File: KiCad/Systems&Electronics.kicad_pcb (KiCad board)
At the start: 2 copper layers, 182.4 x 143.2 mm, 53 parts, among them J1 Pressure Transducer, J12 Screw_Terminal_01x02, J13 Screw_Terminal_01x03, J2 Pressure Transducer, J3 Pressure Transducer, J4 Pressure Transducer, J5 Pressure Transducer, J6 Pressure Transducer

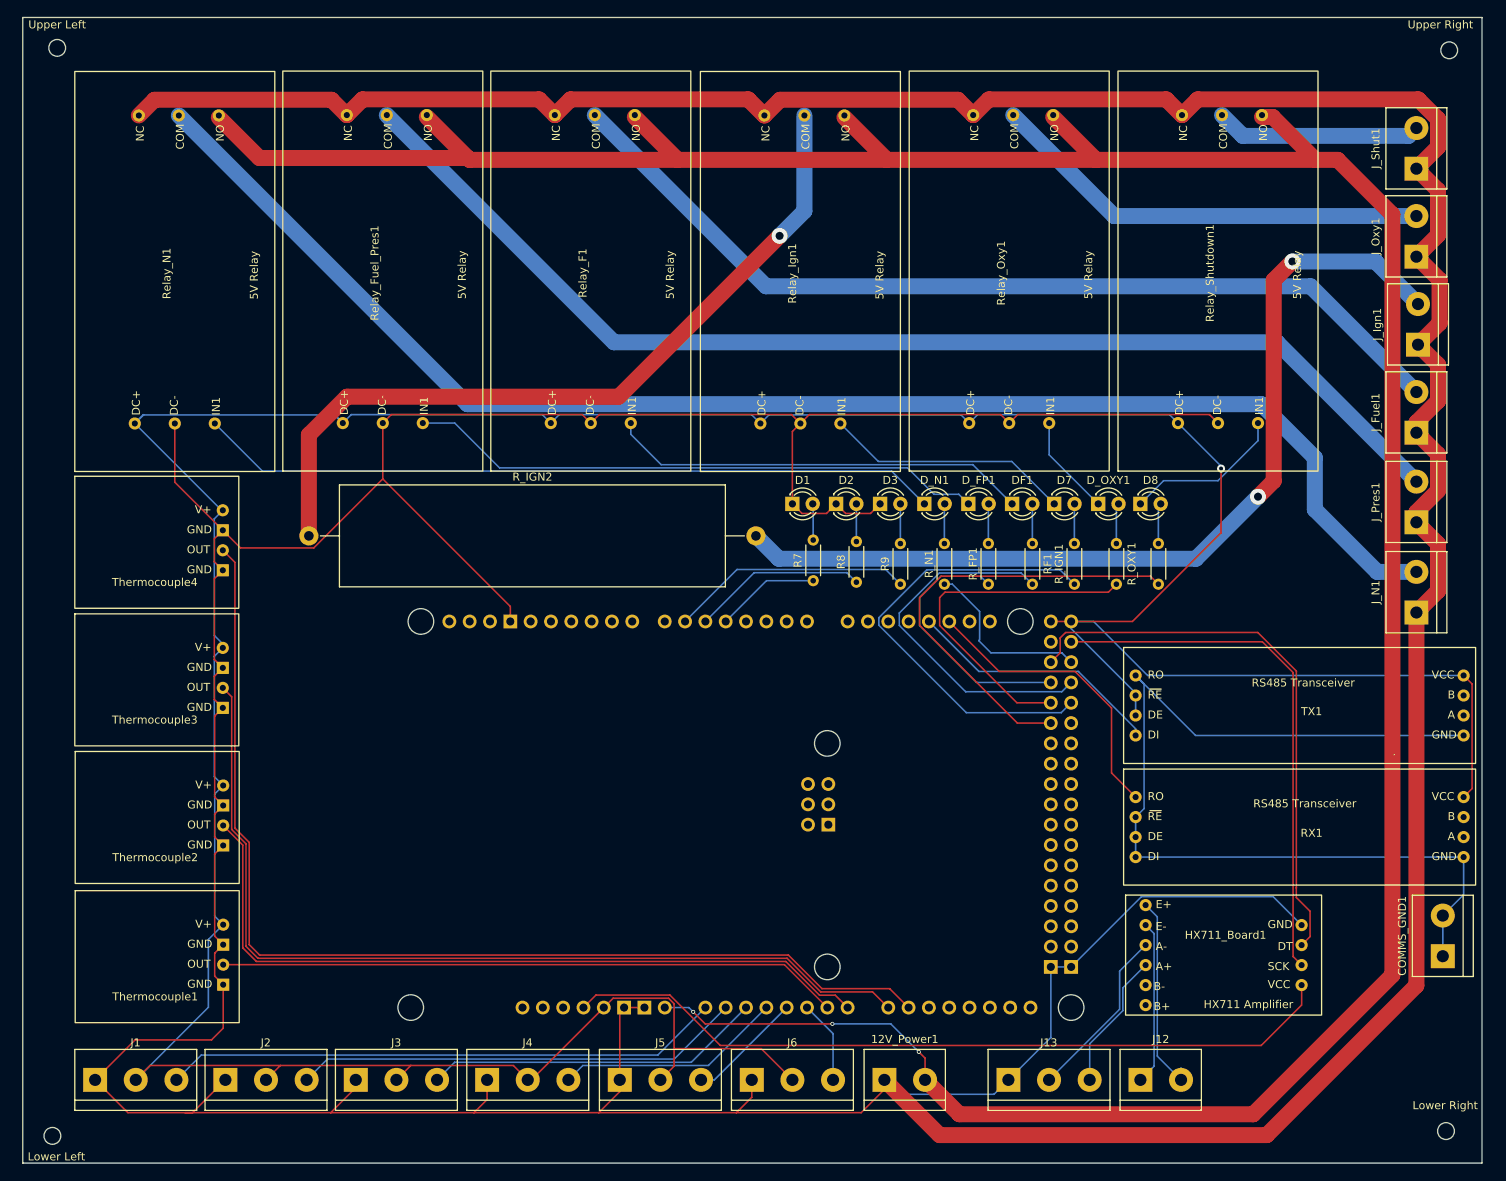
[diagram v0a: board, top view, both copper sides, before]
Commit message: PCB layout minor updates
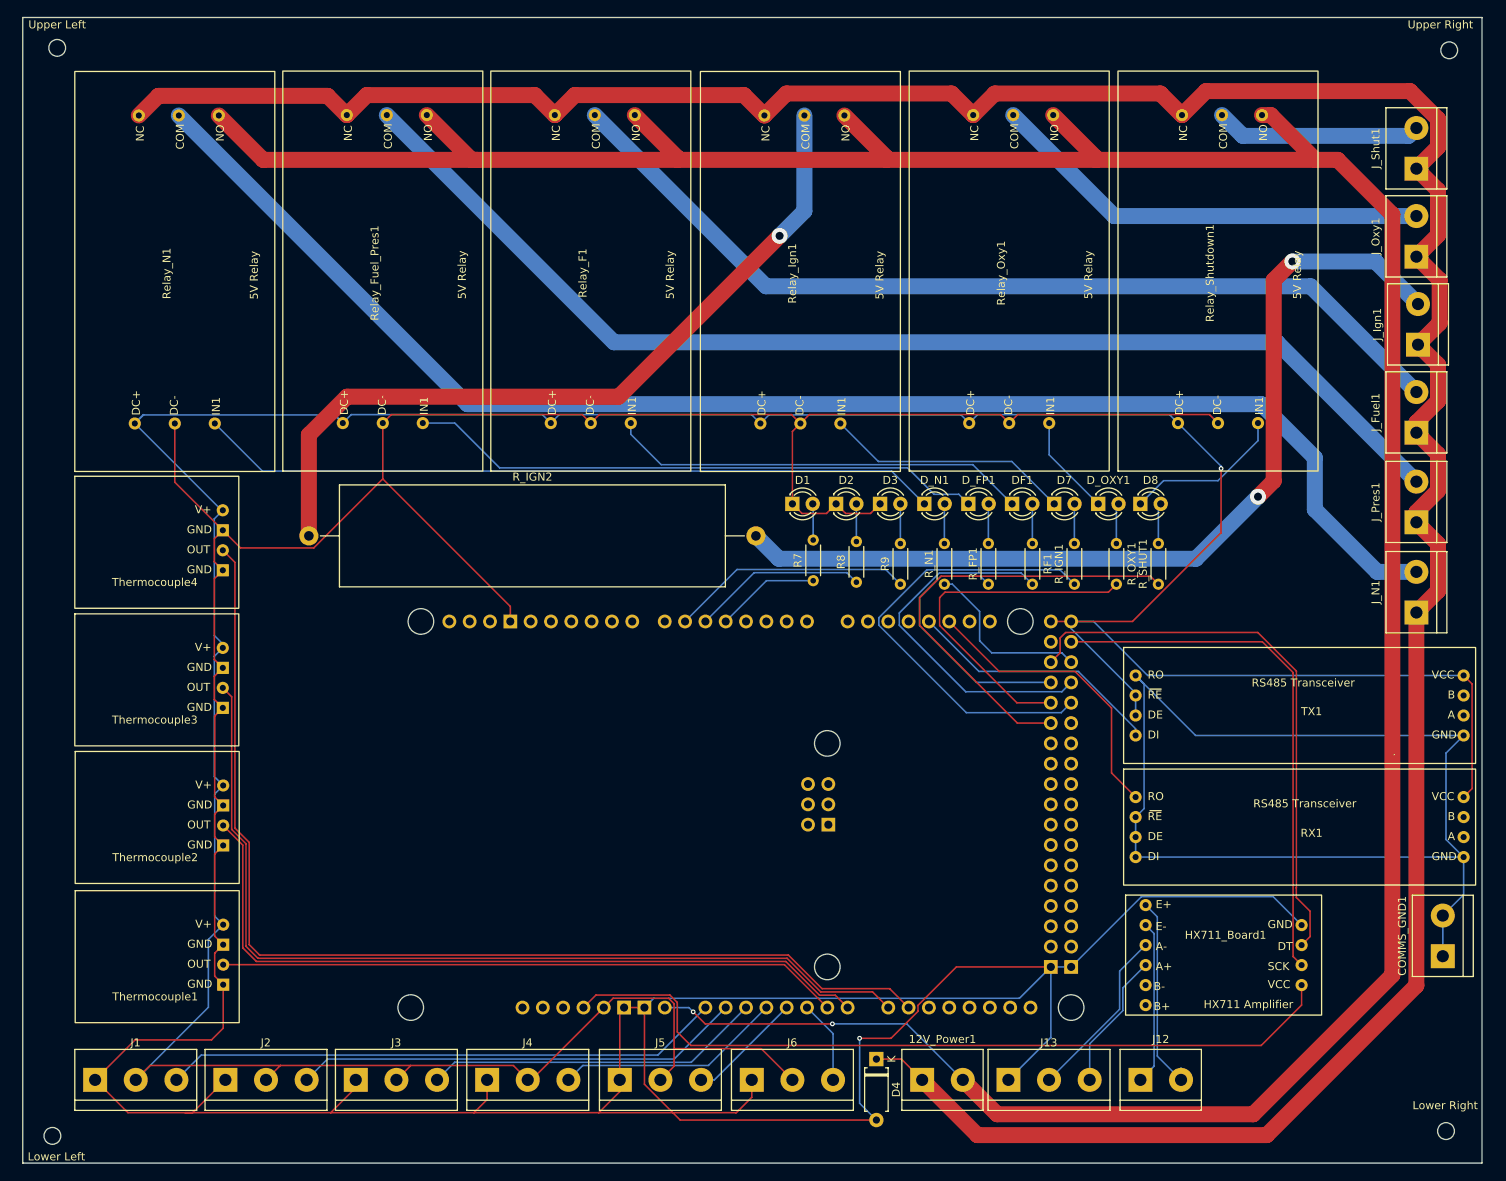
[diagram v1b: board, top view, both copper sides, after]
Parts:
- added D4: D, Diode_THT:D_A-405_P7.62mm_Horizontal, F.Cu at (139.5, 150.4)
- moved 12V_Power1 4.72 mm to (145.2, 153.0)
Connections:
- A1 pad GND1: Net-(12V_Power1-Pin_1) -> Net-(D1-K)
- A1 pad GND2: Net-(12V_Power1-Pin_1) -> Net-(D1-K)
- A1 pad GND3: Net-(12V_Power1-Pin_1) -> Net-(D1-K)
- A1 pad GND5: Net-(12V_Power1-Pin_1) -> Net-(D1-K)
- A1 pad GND6: Net-(12V_Power1-Pin_1) -> Net-(D1-K)
- D1 pad 1: Net-(12V_Power1-Pin_1) -> Net-(D1-K)
- D2 pad 1: Net-(12V_Power1-Pin_1) -> Net-(D1-K)
- D3 pad 1: Net-(12V_Power1-Pin_1) -> Net-(D1-K)
- HX711_Board1 pad GND: Net-(12V_Power1-Pin_1) -> Net-(D1-K)
- J1 pad 1: Net-(12V_Power1-Pin_1) -> Net-(D1-K)
- J13 pad 1: Net-(12V_Power1-Pin_1) -> Net-(D1-K)
- J2 pad 1: Net-(12V_Power1-Pin_1) -> Net-(D1-K)
- J3 pad 1: Net-(12V_Power1-Pin_1) -> Net-(D1-K)
- J4 pad 1: Net-(12V_Power1-Pin_1) -> Net-(D1-K)
- J5 pad 1: Net-(12V_Power1-Pin_1) -> Net-(D1-K)
- J6 pad 1: Net-(12V_Power1-Pin_1) -> Net-(D1-K)
- Relay_F1 pad DC-: Net-(12V_Power1-Pin_1) -> Net-(D1-K)
- Relay_Fuel_Pres1 pad DC-: Net-(12V_Power1-Pin_1) -> Net-(D1-K)
- Relay_Ign1 pad DC-: Net-(12V_Power1-Pin_1) -> Net-(D1-K)
- Relay_N1 pad DC-: Net-(12V_Power1-Pin_1) -> Net-(D1-K)
- Relay_Oxy1 pad DC-: Net-(12V_Power1-Pin_1) -> Net-(D1-K)
- Relay_Shutdown1 pad DC-: Net-(12V_Power1-Pin_1) -> Net-(D1-K)
- Thermocouple1 pad GND: Net-(12V_Power1-Pin_1) -> Net-(D1-K)
- Thermocouple2 pad GND: Net-(12V_Power1-Pin_1) -> Net-(D1-K)
- Thermocouple3 pad GND: Net-(12V_Power1-Pin_1) -> Net-(D1-K)
- Thermocouple4 pad GND: Net-(12V_Power1-Pin_1) -> Net-(D1-K)
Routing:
- net Net-(D1-K): track 0.00 -> 596.0 mm, vias 0 -> 1
- net Net-(12V_Power1-Pin_1): track 871.5 -> 375.5 mm
- net Net-(COMMS_GND1-Pin_1): track 122.2 -> 139.2 mm
- net Net-(A1-3.3V): track 97.6 -> 99.8 mm
- net Net-(12V_Power1-Pin_2): track 391.3 -> 391.6 mm, vias 3 -> 2

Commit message: Footprint and PCB updates
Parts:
- R_IGN2: footprint Resistor_THT:R_Axial_Power_L48.0mm_W12.5mm_P55.88mm -> Resistor_THT:R_Axial_Power_L50.0mm_W9.0mm_P55.88mm
- moved Relay_Shutdown1 3.80 mm to (185.5, 52.0)
- moved Relay_Oxy1 3.15 mm to (158.8, 52.0)
- moved Relay_Ign1 2.51 mm to (132.0, 52.0)
- moved Relay_F1 1.96 mm to (105.2, 52.0)
- moved Relay_Fuel_Pres1 1.21 mm to (78.5, 52.0)
- moved Lower Left 0.74 mm to (36.9, 159.3)
- moved Relay_N1 0.49 mm to (51.8, 52.0)
- moved Lower Right 0.45 mm to (211.2, 159.3)
- moved Upper Left 0.35 mm to (36.9, 24.2)
- moved HX711_Board1 0.35 mm to (183.5, 135.4)
- moved J_Ign1 0.22 mm to (207.0, 61.1)
- moved Upper Right 0.07 mm to (211.2, 24.2)
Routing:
- net Net-(D1-K): track 596.0 -> 638.8 mm
- net Net-(12V_Power1-Pin_1): track 375.5 -> 394.1 mm
- net Net-(D8-K): track 20.2 -> 27.2 mm
- net Net-(12V_Power1-Pin_2): track 391.6 -> 388.4 mm
- net Net-(J_Shut1-Pin_2): track 25.8 -> 22.6 mm
- net Net-(J_N1-Pin_2): track 182.1 -> 185.1 mm
- net Net-(DF1-K): track 52.7 -> 50.0 mm
- net Net-(J_Oxy1-Pin_2): track 55.6 -> 53.0 mm
- net Net-(D7-K): track 30.9 -> 28.5 mm
- net Net-(J_Fuel1-Pin_2): track 117.0 -> 115.6 mm
- net Net-(D_OXY1-K): track 12.6 -> 11.5 mm
- net Net-(D_FP1-K): track 72.4 -> 71.2 mm
- net Net-(J1-Pin_2): track 461.6 -> 460.7 mm, vias 1 -> 0
- net Net-(R_IGN2-Pad1): track 98.1 -> 98.9 mm
- net Net-(J_Pres1-Pin_2): track 147.7 -> 146.9 mm
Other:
- board text added: "A 25mm clearance between the bottom of the PCB and the mount would be optimal if we need to reprogram the Arduino at any point."
- board text added: "Rensselaer Spaceflight Society"
- board text added: "The board itself is about 1.6mm thick"
- board text added: "The corner holes are all the same size and spacing from the edge."
